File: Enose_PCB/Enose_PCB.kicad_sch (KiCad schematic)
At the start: 46 parts, among them IC3 TPS22958DGNR, J1 Conn_01x04_Pin, J10 Fan, J2 Conn_01x04_Pin, J3 Conn_01x04_Pin, J4 DA15_Pins, Q6 NMOS, SW1 SW_SPST, SW2 SW_SPST, SW4 SW_SPDT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

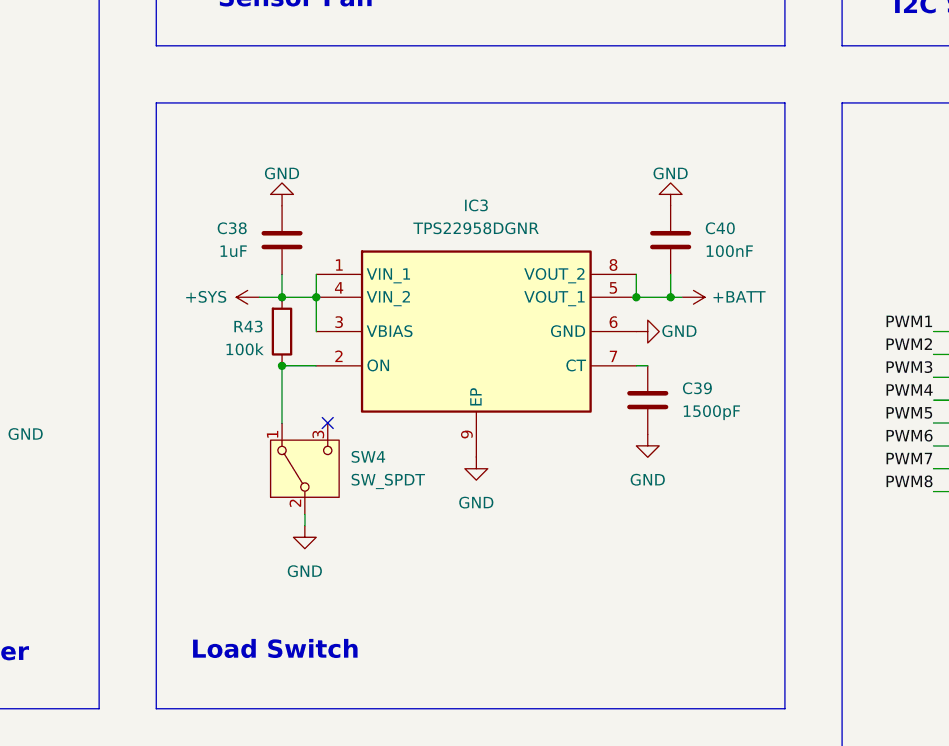
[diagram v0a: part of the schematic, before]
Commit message: Changed power symbols
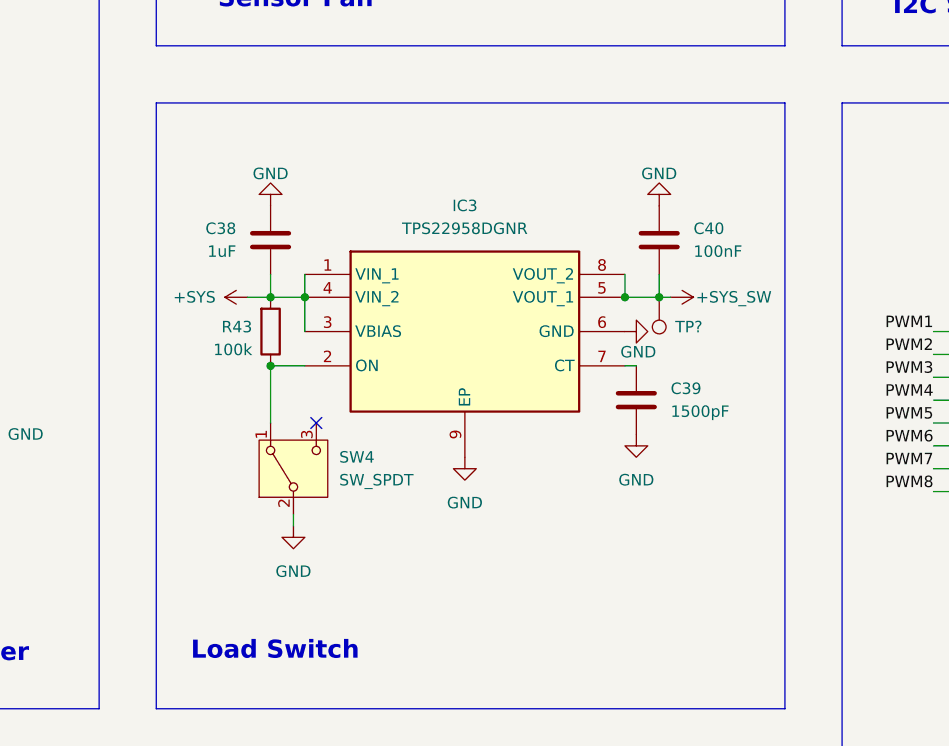
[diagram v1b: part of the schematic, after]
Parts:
- added TP?: TestPoint, TestPoint:TestPoint_Pad_1.5x1.5mm, symbol Connector:TestPoint
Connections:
- net +BATT renamed +SYS_SW
- net +SYS_SW: now also TP?.1
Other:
- moved on the sheet: C38, C39, C40, IC3, R43, SW4

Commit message: Working on Enose PCB Layout
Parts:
- added F1: Fuse Holder, SamacSys_Parts:64600001223, symbol SamacSys_Parts:64600001223
- gave numbers to parts that had none: 1
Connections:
- net +15V: now also F1.1; no longer D8.1 (A1), J4.15 (P15), J4.7, J4.8
- new net: D8.1 (A1), F1.2, J4.15 (P15), J4.7, J4.8
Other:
- moved on the sheet: D8
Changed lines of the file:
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@@
 	)
 	(junction
+		(at 241.3 92.71)
+		(diameter 0)
+		(color 0 0 0 0)
+	)
+	(junction
 		(at 52.07 53.34)
 		(diameter 0)
@@
 	)
 	(junction
-		(at 240.03 92.71)
-		(diameter 0)
-		(color 0 0 0 0)
-	)
-	(junction
 		(at 67.31 43.18)
 		(diameter 0)
@@
 	)
 	(junction
-		(at 52.07 38.1)
+		(at 241.3 101.6)
 		(diameter 0)
 		(color 0 0 0 0)
 	)
 	(junction
-		(at 240.03 101.6)
+		(at 52.07 38.1)
 		(diameter 0)
 		(color 0 0 0 0)
@@
 	(wire
 		(pts
-			(xy 234.95 92.71) (xy 240.03 92.71)
+			(xy 223.52 54.61) (xy 231.14 54.61)
 		)
 		(stroke
@@
 	(wire
 		(pts
-			(xy 223.52 54.61) (xy 231.14 54.61)
+			(xy 48.26 93.98) (xy 52.07 93.98)
 		)
 		(stroke
@@
 	(wire
 		(pts
-			(xy 48.26 93.98) (xy 52.07 93.98)
+			(xy 181.61 48.26) (xy 181.61 46.99)
 		)
 		(stroke
@@
 	(wire
 		(pts
-			(xy 181.61 48.26) (xy 181.61 46.99)
+			(xy 38.1 135.89) (xy 38.1 138.43)
 		)
 		(stroke
@@
 	(wire
 		(pts
-			(xy 38.1 135.89) (xy 38.1 138.43)
+			(xy 238.76 92.71) (xy 241.3 92.71)
 		)
 		(stroke
@@
 	(wire
 		(pts
-			(xy 240.03 100.33) (xy 240.03 101.6)
-		)
-		(stroke
-			(width 0)
-			(type default)
-		)
-	)
-	(wire
-		(pts
 			(xy 143.51 104.14) (xy 143.51 107.95)
 		)
@@
 	(wire
 		(pts
+			(xy 241.3 92.71) (xy 246.38 92.71)
+		)
+		(stroke
+			(width 0)
+			(type default)
+		)
+	)
+	(wire
+		(pts
 			(xy 234.95 115.57) (xy 234.95 129.54)
 		)
@@
 	(wire
 		(pts
-			(xy 40.64 54.61) (xy 40.64 60.96)
+			(xy 241.3 100.33) (xy 241.3 101.6)
 		)
 		(stroke
@@
 	(wire
 		(pts
-			(xy 156.21 39.37) (xy 158.75 39.37)
+			(xy 40.64 54.61) (xy 40.64 60.96)
 		)
 		(stroke
@@
 	(wire
 		(pts
-			(xy 247.65 59.69) (xy 248.92 59.69)
+			(xy 156.21 39.37) (xy 158.75 39.37)
 		)
 		(stroke
@@
 	(wire
 		(pts
-			(xy 213.36 113.03) (xy 215.9 113.03)
+			(xy 247.65 59.69) (xy 248.92 59.69)
 		)
 		(stroke
@@
 	(wire
 		(pts
-			(xy 48.26 91.44) (xy 52.07 91.44)
+			(xy 213.36 113.03) (xy 215.9 113.03)
 		)
 		(stroke
@@
 	(wire
 		(pts
-			(xy 166.37 44.45) (xy 166.37 46.99)
+			(xy 48.26 91.44) (xy 52.07 91.44)
 		)
 		(stroke
@@
 	(wire
 		(pts
-			(xy 106.68 119.38) (xy 106.68 123.19)
+			(xy 166.37 44.45) (xy 166.37 46.99)
 		)
 		(stroke
@@
 	(wire
 		(pts
-			(xy 53.34 121.92) (xy 62.23 121.92)
+			(xy 106.68 119.38) (xy 106.68 123.19)
 		)
 		(stroke
@@
 	(wire
 		(pts
-			(xy 240.03 92.71) (xy 246.38 92.71)
+			(xy 53.34 121.92) (xy 62.23 121.92)
 		)
 		(stroke
@@
 	(wire
 		(pts
+			(xy 241.3 101.6) (xy 246.38 101.6)
+		)
+		(stroke
+			(width 0)
+			(type default)
+		)
+	)
+	(wire
+		(pts
 			(xy 48.26 76.2) (xy 52.07 76.2)
 		)
@@
 	(wire
 		(pts
-			(xy 234.95 101.6) (xy 240.03 101.6)
+			(xy 233.68 101.6) (xy 241.3 101.6)
 		)
 		(stroke
@@
 	(wire
 		(pts
-			(xy 240.03 101.6) (xy 246.38 101.6)
-		)
-		(stroke
-			(width 0)
-			(type default)
-		)
-	)
-	(wire
-		(pts
 			(xy 143.51 101.6) (xy 143.51 104.14)
 		)
@@
 	(symbol
 		(lib_id "power:GND")
-		(at 234.95 101.6 270)
+		(at 233.68 101.6 270)
 		(unit 1)
 		(exclude_from_sim no)
@@
 		(fields_autoplaced yes)
 		(property "Reference" "#PWR063"
-			(at 228.6 101.6 0)
+			(at 227.33 101.6 0)
 			(effects
 				(font
@@
 		)
 		(property "Value" "GND"
-			(at 231.14 101.5999 90)
+			(at 229.87 101.5999 90)
 			(effects
 				(font
@@
 		)
 		(property "Footprint" ""
-			(at 234.95 101.6 0)
+			(at 233.68 101.6 0)
 			(effects
 				(font
@@
 		)
 		(property "Datasheet" ""
-			(at 234.95 101.6 0)
+			(at 233.68 101.6 0)
 			(effects
 				(font
@@
 		)
 		(property "Description" "Power symbol creates a global label with name \"GND\" , ground"
-			(at 234.95 101.6 0)
+			(at 233.68 101.6 0)
 			(effects
 				(font
@@
 					(size 1.27 1.27)
 				)
-				(hide yes)
 			)
 		)
@@
 					(size 1.27 1.27)
 				)
-				(hide yes)
 			)
 		)
@@
 	)
 	(symbol
+		(lib_id "SamacSys_Parts:64600001223")
+		(at 220.98 92.71 0)
+		(unit 1)
+		(exclude_from_sim no)
+		(in_bom yes)
+		(on_board yes)
+		(dnp no)
+		(fields_autoplaced yes)
+		(property "Reference" "F1"
+			(at 229.87 86.36 0)
+			(effects
+				(font
+					(size 1.27 1.27)
+				)
+			)
+		)
+		(property "Value" "Fuse Holder"
+			(at 229.87 88.9 0)
+			(effects
+				(font
+					(size 1.27 1.27)
+				)
+			)
+		)
+		(property "Footprint" "SamacSys_Parts:64600001223"
+			(at 234.95 188.9 0)
+			(effects
+				(font
+					(size 1.27 1.27)
+				)
+				(justify left top)
+				(hide yes)
+			)
+		)
+		(property "Datasheet" "https://m.littelfuse.com/~/media/electronics/datasheets/fuse_blocks/littelfuse_fuse_block_646_datasheet.pdf.pdf"
+			(at 234.95 288.9 0)
+			(effects
+				(font
+					(size 1.27 1.27)
+				)
+				(justify left top)
+				(hide yes)
+			)
+		)
+		(property "Description" "LITTELFUSE - 64600001223 - FUSE BLOCK, 5X20MM, THROUGH HOLE"
+			(at 220.98 92.71 0)
+			(effects
+				(font
+					(size 1.27 1.27)
+				)
+				(hide yes)
+			)
+		)
+		(property "Height" "12"
+			(at 234.95 488.9 0)
+			(effects
+				(font
+					(size 1.27 1.27)
+				)
+				(justify left top)
+				(hide yes)
+			)
+		)
+		(property "Mouser Part Number" "576-64600001223"
+			(at 234.95 588.9 0)
+			(effects
+				(font
+					(size 1.27 1.27)
+				)
+				(justify left top)
+				(hide yes)
+			)
+		)
+		(property "Mouser Price/Stock" "https://www.mouser.co.uk/ProductDetail/Littelfuse/64600001223?qs=up76HT6PtJjfTS5uVso6wg%3D%3D"
+			(at 234.95 688.9 0)
+			(effects
+				(font
+					(size 1.27 1.27)
+				)
+				(justify left top)
+				(hide yes)
+			)
+		)
+		(property "Manufacturer_Name" "LITTELFUSE"
+			(at 234.95 788.9 0)
+			(effects
+				(font
+					(size 1.27 1.27)
+				)
+				(justify left top)
+				(hide yes)
+			)
+		)
+		(property "Manufacturer_Part_Number" "64600001223"
+			(at 234.95 888.9 0)
+			(effects
+				(font
+					(size 1.27 1.27)
+				)
+				(justify left top)
+				(hide yes)
+			)
+		)
+		(pin "1"
+		)
+		(pin "2"
+		)
+		(instances
+			(project ""
+				(path "/eef70be0-4107-491c-8ca0-465071a6397e"
+					(reference "F1")
+					(unit 1)
+				)
+			)
+		)
+	)
+	(symbol
 		(lib_id "Device:C")
 		(at 231.14 58.42 0)
@@
 	(symbol
 		(lib_id "power:+15V")
-		(at 234.95 92.71 90)
+		(at 220.98 92.71 90)
 		(unit 1)
 		(exclude_from_sim no)
@@
 		(fields_autoplaced yes)
 		(property "Reference" "#PWR062"
-			(at 238.76 92.71 0)
+			(at 224.79 92.71 0)
 			(effects
 				(font
@@
 		)
 		(property "Value" "+15V"
-			(at 231.14 92.7099 90)
+			(at 217.17 92.7099 90)
 			(effects
 				(font
@@
 		)
 		(property "Footprint" ""
-			(at 234.95 92.71 0)
+			(at 220.98 92.71 0)
 			(effects
 				(font
@@
 		)
 		(property "Datasheet" ""
-			(at 234.95 92.71 0)
+			(at 220.98 92.71 0)
 			(effects
 				(font
@@
 		)
 		(property "Description" "Power symbol creates a global label with name \"+15V\""
-			(at 234.95 92.71 0)
+			(at 220.98 92.71 0)
 			(effects
 				(font
@@
 	(symbol
 		(lib_id "Diode:SM6T18A")
-		(at 240.03 96.52 90)
+		(at 241.3 96.52 90)
 		(mirror x)
 		(unit 1)
@@
 		(dnp no)
 		(property "Reference" "D8"
-			(at 237.49 95.2499 90)
+			(at 238.76 95.2499 90)
 			(effects
 				(font
@@
 		)
 		(property "Value" "SMBJ18A-E3/52"
-			(at 237.49 97.7899 90)
+			(at 238.76 97.7899 90)
 			(effects
 				(font
@@
 		)
 		(property "Footprint" "Diode_SMD:D_SMB"
-			(at 245.11 96.52 0)
+			(at 246.38 96.52 0)
 			(effects
 				(font
@@
 		)
 		(property "Datasheet" "http://www.vishay.com/docs/88392/smbj.pdf"
-			(at 240.03 95.25 0)
+			(at 241.3 95.25 0)
 			(effects
 				(font
@@
 		)
 		(property "Description" "Vishay SMBJ18A-E3/52, Uni-Directional TVS Diode, 600W, 2-Pin DO-214AA"
-			(at 240.03 96.52 0)
+			(at 241.3 96.52 0)
 			(effects
 				(font
@@
 		(on_board yes)
 		(dnp no)
-		(property "Reference" "TP?"
+		(property "Reference" "TP7"
 			(at 184.658 107.442 0)
 			(effects
@@
 			(project "Enose_PCB"
 				(path "/eef70be0-4107-491c-8ca0-465071a6397e"
-					(reference "TP?")
+					(reference "TP7")
 					(unit 1)
 				)

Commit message: Finished placeing components for Enose PCB
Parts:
- added H1, H2, H3, H4: MountingHole, MountingHole:MountingHole_2.5mm, symbol Mechanical:MountingHole
- added J11: Conn_01x04_Pin, symbol Connector:Conn_01x04_Pin
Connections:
- net ESP_LED1: now also U1.34 (IO41); no longer U1.6 (IO6)
- net ESP_LED2: now also U1.35 (IO42); no longer U1.7 (IO7)
- net Fan PWM: now also U1.9 (IO16); no longer U1.12 (IO8)
- net I2C_SCL: now also R33.1, U1.38 (IO2); no longer R31.1, U1.27 (IO0)
- net PWM1: now also R42.1; no longer R35.1
- net PWM2: now also R41.1; no longer R36.1
- net PWM3: now also R40.1; no longer R37.1
- net PWM4: now also R39.1; no longer R38.1
- net PWM5: now also R38.1; no longer R39.1
- net PWM6: now also R37.1; no longer R40.1
- net PWM7: now also R36.1, U1.23 (IO21); no longer R41.1, U1.8 (IO15)
- net PWM8: now also R35.1, U1.24 (IO47); no longer R42.1, U1.9 (IO16)
- net ~{INT}: now also R31.1, U1.31 (IO38); no longer R33.1, U1.38 (IO2)
- net at U1.15 (IO3): no longer SW2.4 (B)
- net at U1.25 (IO48): now also SW2.4 (B)
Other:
- moved on the sheet: R31, SW2

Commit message: Enose PCB almost done
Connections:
- net +3V3: now also J1.1 (Pin_1), J2.1 (Pin_1), J3.1 (Pin_1); no longer J1.4 (Pin_4), J2.4 (Pin_4), J3.4 (Pin_4)
- net EN(15V): now also U1.8 (IO15); no longer U1.11 (IO18)
- net GND: now also J1.2 (Pin_2), J2.2 (Pin_2), J3.2 (Pin_2); no longer J1.3 (Pin_3), J2.3 (Pin_3), J3.3 (Pin_3)
- net I2C_SCL: now also J1.4 (Pin_4), J2.4 (Pin_4), J3.4 (Pin_4), U1.12 (IO8); no longer J1.2 (Pin_2), J2.2 (Pin_2), J3.2 (Pin_2), U1.38 (IO2)
- net I2C_SDA: now also J1.3 (Pin_3), J2.3 (Pin_3), J3.3 (Pin_3), U1.11 (IO18); no longer J1.1 (Pin_1), J2.1 (Pin_1), J3.1 (Pin_1), U1.39 (IO1)
- net PWRKEY: now also U1.39 (IO1); no longer U1.10 (IO17)
- net UART1_RXD: now also R2.2, U1.36 (RXD0); no longer U1.37 (TXD0)
- net UART1_TXD: now also U1.37 (TXD0); no longer R2.2, U1.36 (RXD0)
- net ~{INT}: now also U1.10 (IO17); no longer U1.31 (IO38)
- net at U1.25 (IO48): no longer SW2.4 (B)
- net at U1.27 (IO0): now also SW2.4 (B)
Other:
- moved on the sheet: C1, C2, C3, C4, D1, D14, J1, J11, J2, J3, R1, R2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

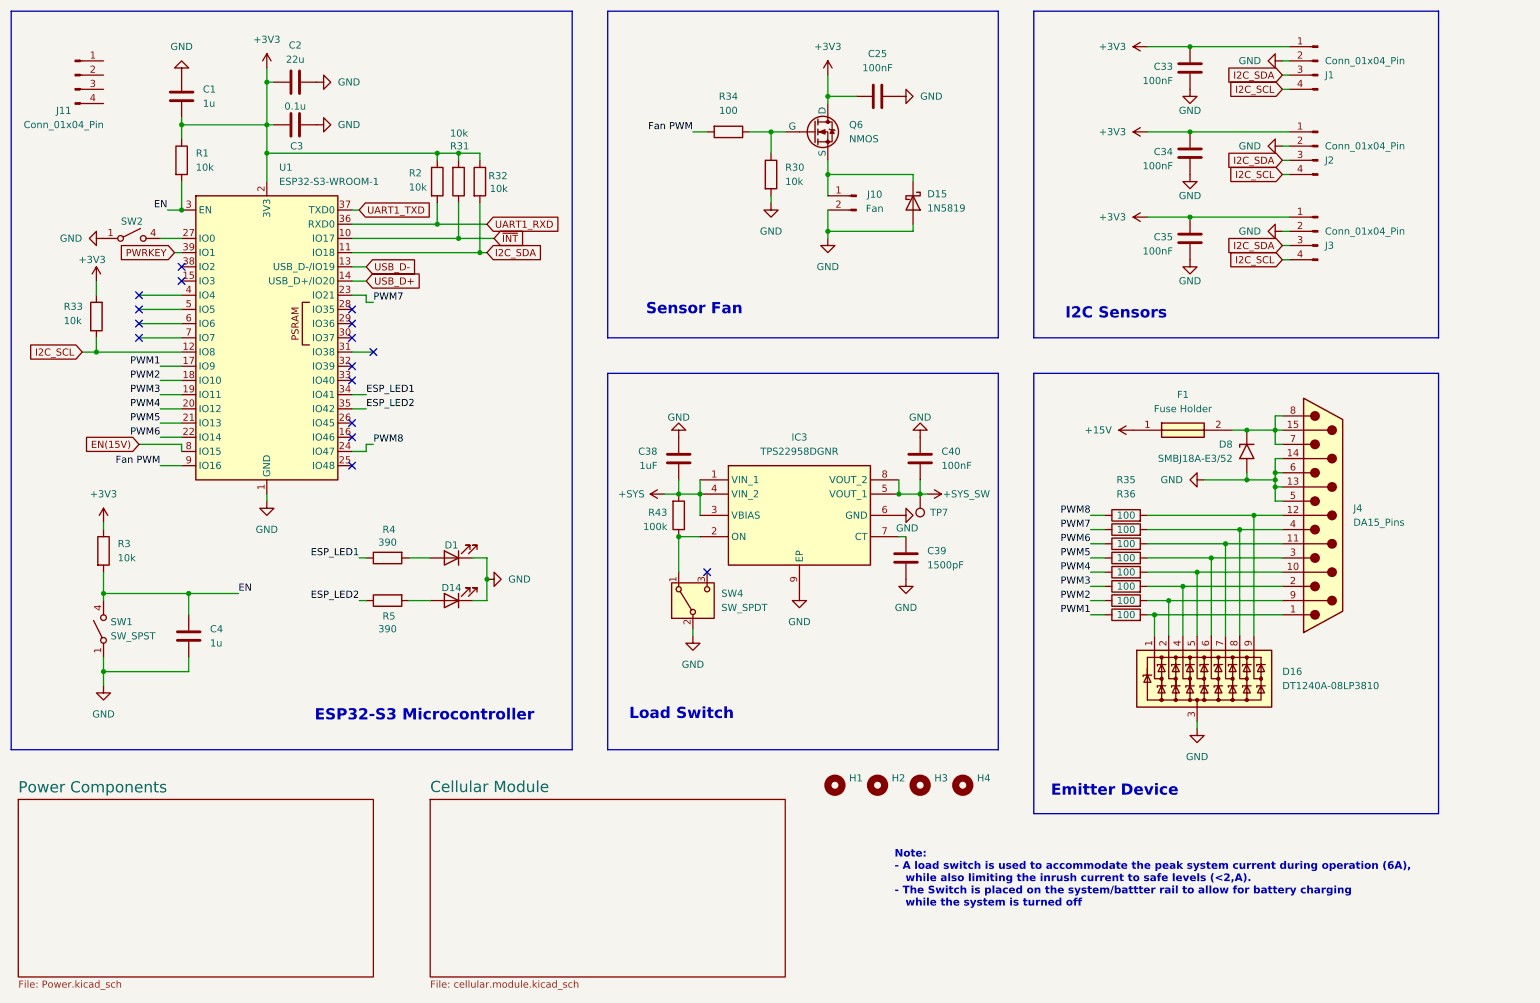
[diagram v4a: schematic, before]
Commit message: Enose PCB almost done, just needs ground vias
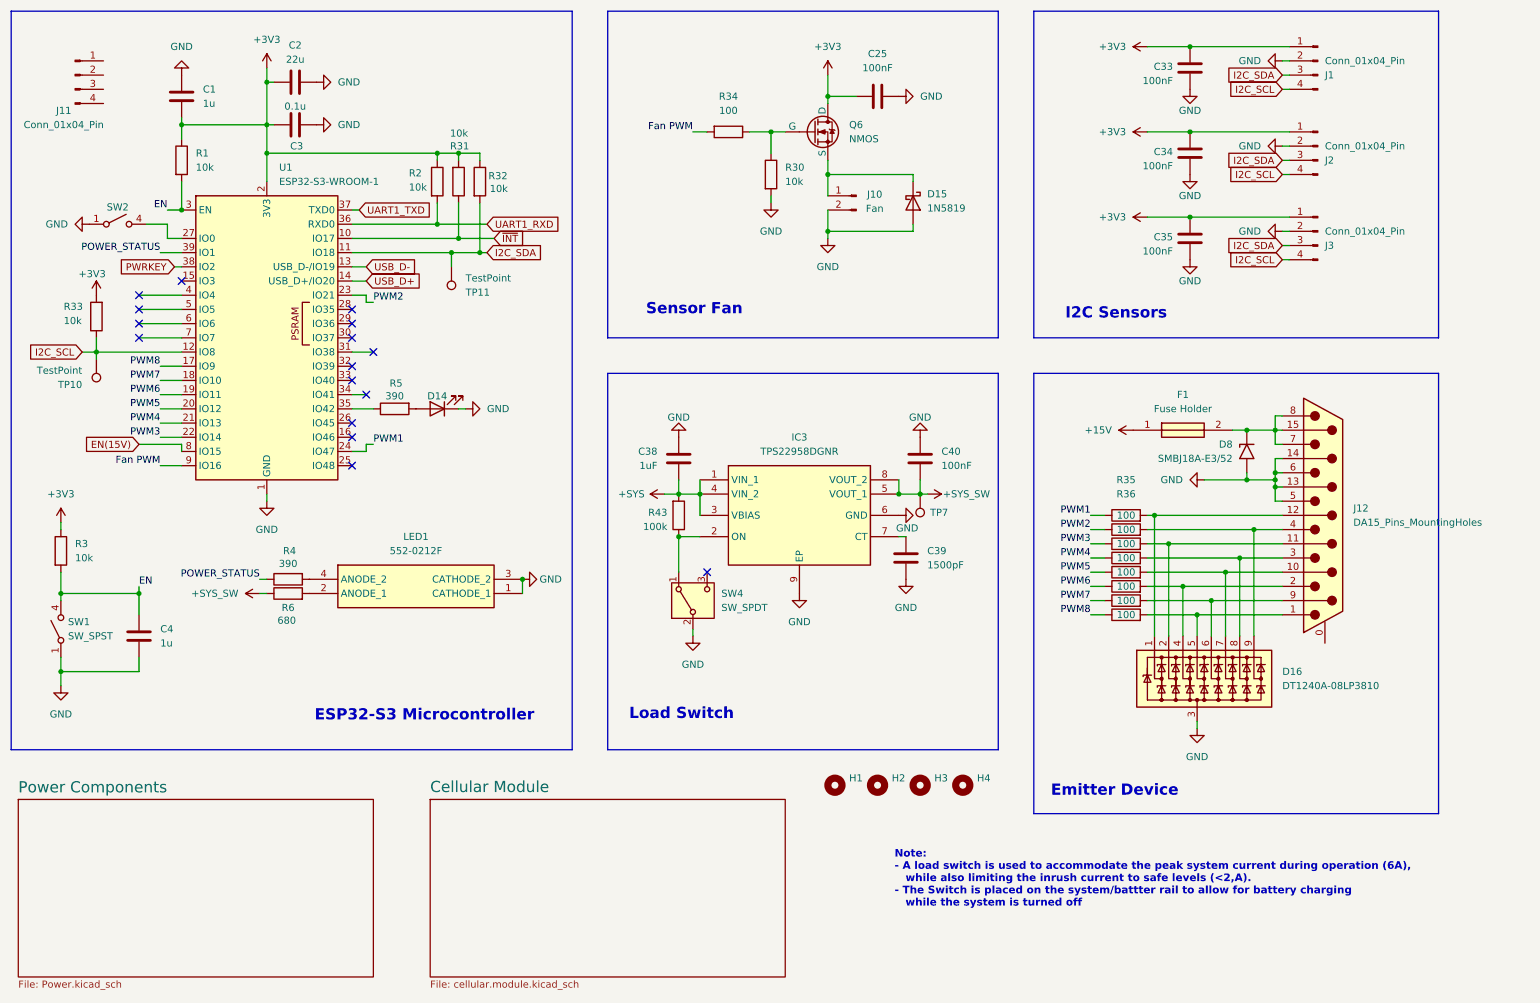
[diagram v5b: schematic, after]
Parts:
- removed D1: LED Amber, LED_SMD:LED_0805_2012Metric_Pad1.15x1.40mm_HandSolder, symbol Device:LED
- removed J4: DA15_Pins, Connector_Dsub:DSUB-15_Pins_Horizontal_P2.77x2.84mm_EdgePinOffset9.40mm, symbol Connector:DA15_Pins
- added J12: DA15_Pins_MountingHoles, SamacSys_Parts:6E17C015PAJ121, symbol Connector:DA15_Pins_MountingHoles
- added LED1: 552-0212F, SamacSys_Parts:5520212F, symbol SamacSys_Parts:552-0212F
- added R6: 680, Resistor_SMD:R_0805_2012Metric_Pad1.20x1.40mm_HandSolder, symbol Device:R
- added TP10, TP11: TestPoint, TestPoint:TestPoint_Pad_D1.5mm, symbol Connector:TestPoint
- H1, H2, H3, H4: footprint MountingHole:MountingHole_2.5mm -> MountingHole:MountingHole_3.2mm_M3
- TP7: footprint TestPoint:TestPoint_Pad_1.5x1.5mm -> TestPoint:TestPoint_Pad_D1.5mm
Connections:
- net +SYS_SW: now also R6.1
- net GND: now also J12.13 (P13), J12.14 (P14), J12.5, J12.6, LED1.1 (CATHODE_1), LED1.3 (CATHODE_2)
- net I2C_SCL: now also TP10.1
- net I2C_SDA: now also TP11.1
- net PWM1: now also R35.1, U1.24 (IO47); no longer R42.1, U1.17 (IO9)
- net PWM2: now also R36.1, U1.23 (IO21); no longer R41.1, U1.18 (IO10)
- net PWM3: now also R37.1, U1.22 (IO14); no longer R40.1, U1.19 (IO11)
- net PWM4: now also R38.1, U1.21 (IO13); no longer R39.1, U1.20 (IO12)
- net PWM5: now also R39.1, U1.20 (IO12); no longer R38.1, U1.21 (IO13)
- net PWM6: now also R40.1, U1.19 (IO11); no longer R37.1, U1.22 (IO14)
- net PWM7: now also R41.1, U1.18 (IO10); no longer R36.1, U1.23 (IO21)
- net PWM8: now also R42.1, U1.17 (IO9); no longer R35.1, U1.24 (IO47)
- net PWRKEY: now also U1.38 (IO2); no longer U1.39 (IO1)
- net at R38.2: now also D16.8 (K7), J12.3; no longer D16.6 (K5)
- net at D16.4 (K3), R40.2: now also J12.2
- net at R37.2: now also D16.2 (K2), J12.11 (P111); no longer D16.7 (K6)
- net at R41.2: now also D16.6 (K5), J12.9 (P9); no longer D16.2 (K2)
- net at D16.1 (K1): now also R35.2, J12.12 (P12); no longer R42.2
- net at R39.2: now also D16.7 (K6), J12.10 (P10); no longer D16.5 (K4)
- net at D16.9 (K8): now also R36.2, J12.4; no longer R35.2
- net at D8.1 (A1), F1.2: now also J12.15 (P15), J12.7, J12.8
- net at R4.2: now also LED1.4 (ANODE_2)
- net ESP_LED1: no longer names the net of U1.34 (IO41)
- net ESP_LED1: no longer R4.1
- net ESP_LED2: no longer names the net of R5.1, U1.35 (IO42)
- new net: LED1.2 (ANODE_1), R6.2
- new net: D16.5 (K4), J12.1, R42.2
- new net POWER_STATUS: R4.1, U1.39 (IO1)
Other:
- moved on the sheet: C4, D14, R3, R4, R5, SW1, SW2
